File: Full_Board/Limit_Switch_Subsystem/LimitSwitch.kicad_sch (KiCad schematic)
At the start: 7 parts, among them J7 OQ0212500000G

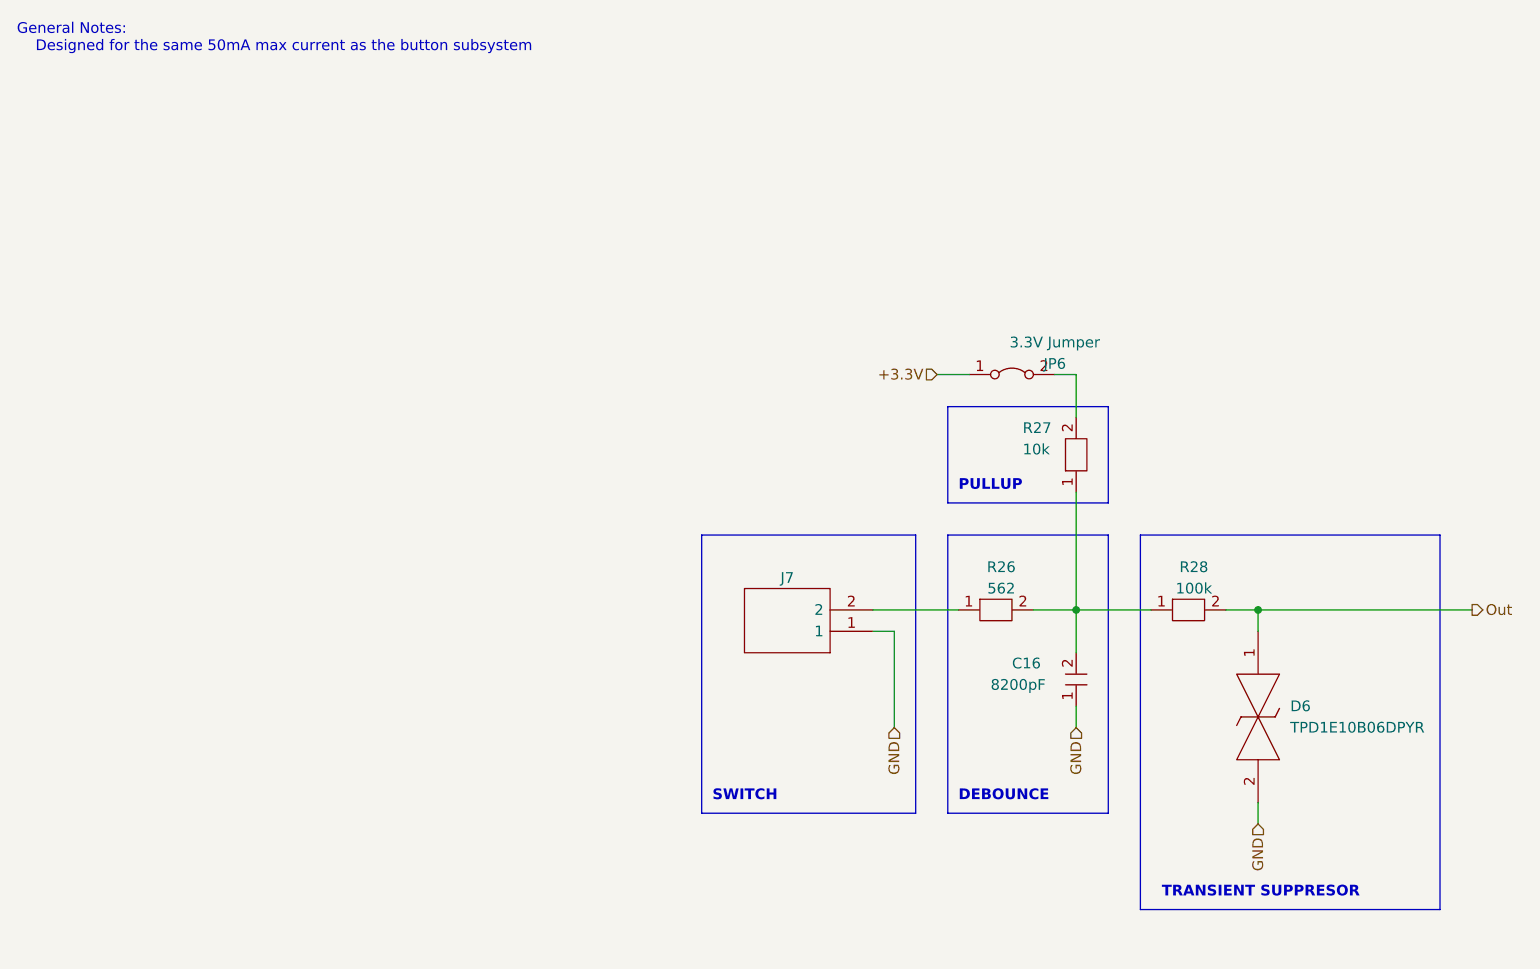
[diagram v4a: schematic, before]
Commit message: Swapped TVS Diodes
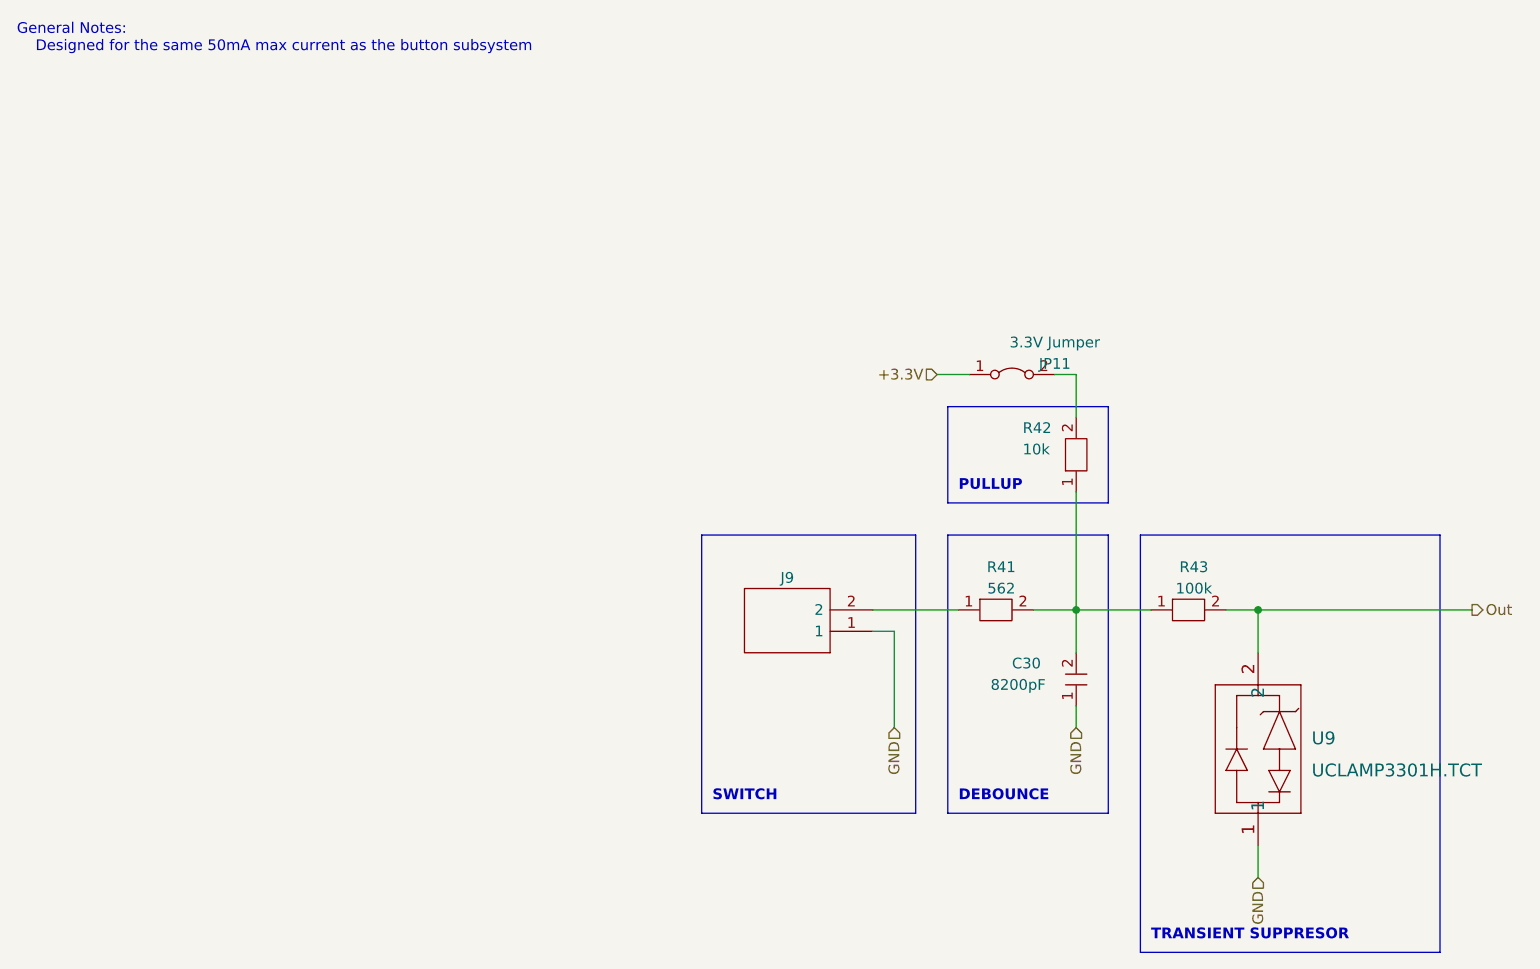
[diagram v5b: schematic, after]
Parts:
- removed D6: TPD1E10B06DPYR, TPD1E10B06DPYR:TPD1E10B06DPYR, symbol TPD1E10B06DPYR:TPD1E10B06DPYR
- added U9: UCLAMP3301H.TCT, SOD_01H.TCT_SEM, symbol UCLAMP3301H-TCT:UCLAMP3301H.TCT
- renumbered C16 to C30, J7 to J9, JP6 to JP11, R26 to R41, R27 to R42, R28 to R43
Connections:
- net GND: now also U9.1
- net Out: now also U9.2
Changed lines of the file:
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@@
     (stroke (width 0) (type default) (color 0 0 0 0))
   )
-  (polyline (pts (xy 151.13 125.73) (xy 186.69 125.73))
+  (polyline (pts (xy 151.13 130.81) (xy 186.69 130.81))
     (stroke (width 0) (type default) (color 0 0 0 0))
   )
@@
     (stroke (width 0) (type default) (color 0 0 0 0))
   )
-  (polyline (pts (xy 151.13 81.28) (xy 151.13 125.73))
+  (wire (pts (xy 165.1 118.11) (xy 165.1 121.92))
+    (stroke (width 0) (type default) (color 0 0 0 0))
+  )
+  (polyline (pts (xy 151.13 81.28) (xy 151.13 130.81))
     (stroke (width 0) (type default) (color 0 0 0 0))
   )
@@
     (stroke (width 0) (type default) (color 0 0 0 0))
   )
-  (wire (pts (xy 165.1 90.17) (xy 165.1 92.71))
-    (stroke (width 0) (type default) (color 0 0 0 0))
-  )
-  (wire (pts (xy 165.1 113.03) (xy 165.1 115.57))
+  (wire (pts (xy 165.1 90.17) (xy 165.1 95.25))
     (stroke (width 0) (type default) (color 0 0 0 0))
   )
@@
     (stroke (width 0) (type default) (color 0 0 0 0))
   )
-  (polyline (pts (xy 186.69 125.73) (xy 186.69 81.28))
+  (polyline (pts (xy 186.69 130.81) (xy 186.69 81.28))
     (stroke (width 0) (type default) (color 0 0 0 0))
   )
@@
     (effects (font (size 1.27 1.27) bold) (justify left bottom))
   )
-  (text "TRANSIENT SUPPRESOR" (at 153.67 124.46 0)
+  (text "TRANSIENT SUPPRESOR" (at 152.4 129.54 0)
     (effects (font (size 1.27 1.27) bold) (justify left bottom))
   )
@@
     (effects (font (size 1.27 1.27)) (justify left))
   )
-  (hierarchical_label "GND" (shape input) (at 165.1 115.57 270)
+  (hierarchical_label "GND" (shape input) (at 165.1 121.92 270)
     (effects (font (size 1.27 1.27)) (justify right))
   )
   (symbol (lib_id "OQ0212500000G:OQ0212500000G") (at 119.38 92.71 180)
     (in_bom yes) (on_board yes)
-    (property "Reference" "J7" (id 0) (at 109.22 86.36 0))
+    (property "Reference" "J9" (id 0) (at 109.22 86.36 0))
     (property "Value" "OQ0212500000G" (id 1) (at 109.22 85.09 0)
       (effects (font (size 1.27 1.27)) hide)
@@
   (symbol (lib_id "CR0402-FX-5620GLF:CR0402-FX-5620GLF") (at 129.54 90.17 0)
     (in_bom yes) (on_board yes)
-    (property "Reference" "R26" (id 0) (at 134.62 85.09 0))
+    (property "Reference" "R41" (id 0) (at 134.62 85.09 0))
     (property "Value" "562" (id 1) (at 134.62 87.63 0))
     (property "Footprint" "CR0402-FX-5620GLF:RESC1005X40N" (id 2) (at 143.51 88.9 0)
@@
   (symbol (lib_id "RMCF1206FT10K0:10k") (at 143.51 76.2 90)
     (in_bom yes) (on_board yes)
-    (property "Reference" "R27" (id 0) (at 137.16 68.58 90)
+    (property "Reference" "R42" (id 0) (at 137.16 68.58 90)
       (effects (font (size 1.27 1.27)) (justify right))
     )
@@
   (symbol (lib_id "RCV2512100KFKEGAT:RCV2512100KFKEGAT") (at 152.4 90.17 0)
     (in_bom yes) (on_board yes)
-    (property "Reference" "R28" (id 0) (at 157.48 85.09 0))
+    (property "Reference" "R43" (id 0) (at 157.48 85.09 0))
     (property "Value" "100k" (id 1) (at 157.48 87.63 0))
     (property "Footprint" "RCV2512100KFKEGAT:RESC6332X70N" (id 2) (at 166.37 88.9 0)
@@
   (symbol (lib_id "C1210C822K2RACAUTO:C1210C822K2RACAUTO") (at 143.51 101.6 90)
     (in_bom yes) (on_board yes)
-    (property "Reference" "C16" (id 0) (at 135.89 96.52 90)
+    (property "Reference" "C30" (id 0) (at 135.89 96.52 90)
       (effects (font (size 1.27 1.27)) (justify right))
     )
@@
   (symbol (lib_id "Jumper:Jumper_2_Bridged") (at 135.89 62.23 0)
     (in_bom yes) (on_board yes)
-    (property "Reference" "JP6" (id 0) (at 140.97 60.96 0))
+    (property "Reference" "JP11" (id 0) (at 140.97 60.96 0))
     (property "Value" "3.3V Jumper" (id 1) (at 140.97 58.42 0))
     (property "Footprint" "TestPoint:TestPoint_2Pads_Pitch2.54mm_Drill0.8mm" (id 2) (at 135.89 62.23 0)
@@
     (pin "2")
   )
-  (symbol (lib_id "TPD1E10B06DPYR:TPD1E10B06DPYR") (at 165.1 92.71 270)
-    (in_bom yes) (on_board yes)
-    (property "Reference" "D6" (id 0) (at 168.91 101.6 90)
-      (effects (font (size 1.27 1.27)) (justify left))
-    )
-    (property "Value" "TPD1E10B06DPYR" (id 1) (at 168.91 104.1399 90)
-      (effects (font (size 1.27 1.27)) (justify left))
-    )
-    (property "Footprint" "TPD1E10B06DPYR:TPD1E10B06DPYR" (id 2) (at 168.91 105.41 0)
-      (effects (font (size 1.27 1.27)) (justify left bottom) hide)
-    )
-    (property "Datasheet" "https://www.ti.com/lit/ds/symlink/tpd1e10b06.pdf?HQS=dis-mous-null-mousermode-dsf-pf-null-wwe&ts=1664782336823&ref_url=https%253A%252F%252Feu.mouser.com%252F" (id 3) (at 166.37 105.41 0)
-      (effects (font (size 1.27 1.27)) (justify left bottom) hide)
-    )
-    (property "Manufacturer's Part Number" "TPD1E10B06DPYR" (id 4) (at 151.13 105.41 0)
-      (effects (font (size 1.27 1.27)) (justify left bottom) hide)
-    )
-    (property "Digikey Part Number" "296-30406-1-ND" (id 5) (at 163.83 105.41 0)
-      (effects (font (size 1.27 1.27)) (justify left bottom) hide)
-    )
-    (property "Mouser Part Number" "595-TPD1E10B06DPYR" (id 6) (at 158.75 105.41 0)
-      (effects (font (size 1.27 1.27)) (justify left bottom) hide)
-    )
-    (property "Digikey link" "https://www.digikey.com/en/products/detail/texas-instruments/TPD1E10B06DPYR/3197744" (id 7) (at 156.21 105.41 0)
-      (effects (font (size 1.27 1.27)) (justify left bottom) hide)
-    )
-    (property "Mouser link" "https://www.mouser.com/ProductDetail/Texas-Instruments/TPD1E10B06DPYR?qs=UFc95S4Z4CaJYpQ4xqTc0g%3D%3D" (id 8) (at 153.67 105.41 0)
-      (effects (font (size 1.27 1.27)) (justify left bottom) hide)
-    )
-    (pin "1")
+  (symbol (lib_id "UCLAMP3301H-TCT:UCLAMP3301H.TCT") (at 165.1 127 90)
+    (in_bom yes) (on_board yes) (fields_autoplaced)
+    (property "Reference" "U9" (id 0) (at 171.45 105.41 90)
+      (effects (font (size 1.524 1.524)) (justify right))
+    )
+    (property "Value" "UCLAMP3301H.TCT" (id 1) (at 171.45 109.22 90)
+      (effects (font (size 1.524 1.524)) (justify right))
+    )
+    (property "Footprint" "SOD_01H.TCT_SEM" (id 2) (at 149.86 104.14 0)
+      (effects (font (size 1.524 1.524)) hide)
+    )
+    (property "Datasheet" "https://semtech.my.salesforce.com/sfc/p/#E0000000JelG/a/44000000MDWf/s0KJxyOHQyYOcvBXVBK9X3X8Cxj1gNltZ2vd2k1S0Wo" (id 3) (at 173.99 125.73 0)
+      (effects (font (size 1.524 1.524)) hide)
+    )
+    (property "Manufacturers Part Number" "UCLAMP3301H.TCT" (id 4) (at 151.13 123.19 0)
+      (effects (font (size 1.27 1.27)) hide)
+    )
+    (property "Digikey Part Number" "UCLAMP3301HDKR-ND" (id 5) (at 153.67 124.46 0)
+      (effects (font (size 1.27 1.27)) hide)
+    )
+    (property "Mouser Part Number" "" (id 6) (at 165.1 127 0)
+      (effects (font (size 1.27 1.27)) hide)
+    )
+    (property "Digikey Link" "https://www.digikey.com/en/products/detail/semtech-corporation/UCLAMP3301H-TCT/1000952" (id 7) (at 173.99 125.73 0)
+      (effects (font (size 1.27 1.27)) hide)
+    )
+    (property "Mouser Link" "" (id 8) (at 165.1 127 0)
+      (effects (font (size 1.27 1.27)) hide)
+    )
+    (pin "1")

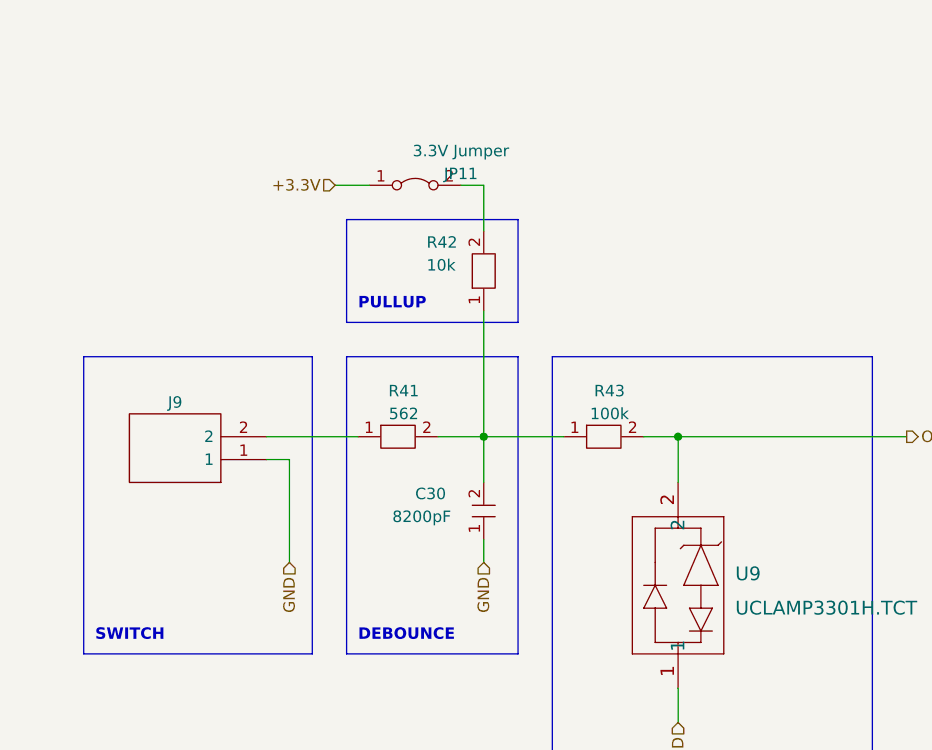
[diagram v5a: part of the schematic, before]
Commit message: Relayed out the power supply and stepper drivers
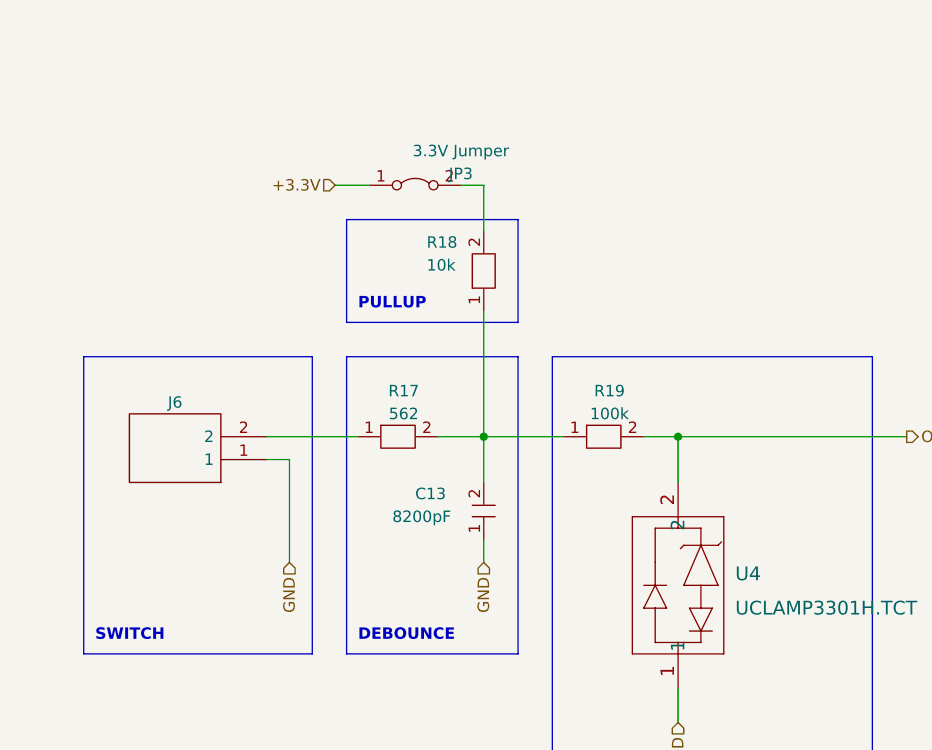
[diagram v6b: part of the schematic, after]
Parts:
- U4: renamed from U9; footprint SOD_01H.TCT_SEM -> UCLAMP3310H-TCT:UCLAMP3301H.TCT
- renumbered C30 to C13, J9 to J6, JP11 to JP3, R41 to R17, R42 to R18, R43 to R19
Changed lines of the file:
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@@
   (symbol (lib_id "OQ0212500000G:OQ0212500000G") (at 119.38 92.71 180)
     (in_bom yes) (on_board yes)
-    (property "Reference" "J9" (id 0) (at 109.22 86.36 0))
+    (property "Reference" "J6" (id 0) (at 109.22 86.36 0))
     (property "Value" "OQ0212500000G" (id 1) (at 109.22 85.09 0)
       (effects (font (size 1.27 1.27)) hide)
@@
   (symbol (lib_id "CR0402-FX-5620GLF:CR0402-FX-5620GLF") (at 129.54 90.17 0)
     (in_bom yes) (on_board yes)
-    (property "Reference" "R41" (id 0) (at 134.62 85.09 0))
+    (property "Reference" "R17" (id 0) (at 134.62 85.09 0))
     (property "Value" "562" (id 1) (at 134.62 87.63 0))
     (property "Footprint" "CR0402-FX-5620GLF:RESC1005X40N" (id 2) (at 143.51 88.9 0)
@@
   (symbol (lib_id "RMCF1206FT10K0:10k") (at 143.51 76.2 90)
     (in_bom yes) (on_board yes)
-    (property "Reference" "R42" (id 0) (at 137.16 68.58 90)
+    (property "Reference" "R18" (id 0) (at 137.16 68.58 90)
       (effects (font (size 1.27 1.27)) (justify right))
     )
@@
   (symbol (lib_id "RCV2512100KFKEGAT:RCV2512100KFKEGAT") (at 152.4 90.17 0)
     (in_bom yes) (on_board yes)
-    (property "Reference" "R43" (id 0) (at 157.48 85.09 0))
+    (property "Reference" "R19" (id 0) (at 157.48 85.09 0))
     (property "Value" "100k" (id 1) (at 157.48 87.63 0))
     (property "Footprint" "RCV2512100KFKEGAT:RESC6332X70N" (id 2) (at 166.37 88.9 0)
@@
   (symbol (lib_id "C1210C822K2RACAUTO:C1210C822K2RACAUTO") (at 143.51 101.6 90)
     (in_bom yes) (on_board yes)
-    (property "Reference" "C30" (id 0) (at 135.89 96.52 90)
+    (property "Reference" "C13" (id 0) (at 135.89 96.52 90)
       (effects (font (size 1.27 1.27)) (justify right))
     )
@@
   (symbol (lib_id "Jumper:Jumper_2_Bridged") (at 135.89 62.23 0)
     (in_bom yes) (on_board yes)
-    (property "Reference" "JP11" (id 0) (at 140.97 60.96 0))
+    (property "Reference" "JP3" (id 0) (at 140.97 60.96 0))
     (property "Value" "3.3V Jumper" (id 1) (at 140.97 58.42 0))
     (property "Footprint" "TestPoint:TestPoint_2Pads_Pitch2.54mm_Drill0.8mm" (id 2) (at 135.89 62.23 0)
@@
   (symbol (lib_id "UCLAMP3301H-TCT:UCLAMP3301H.TCT") (at 165.1 127 90)
     (in_bom yes) (on_board yes) (fields_autoplaced)
-    (property "Reference" "U9" (id 0) (at 171.45 105.41 90)
+    (property "Reference" "U4" (id 0) (at 171.45 105.41 90)
       (effects (font (size 1.524 1.524)) (justify right))
     )
@@
       (effects (font (size 1.524 1.524)) (justify right))
     )
-    (property "Footprint" "SOD_01H.TCT_SEM" (id 2) (at 149.86 104.14 0)
+    (property "Footprint" "UCLAMP3310H-TCT:UCLAMP3301H.TCT" (id 2) (at 149.86 104.14 0)
       (effects (font (size 1.524 1.524)) hide)
     )

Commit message: More layout work
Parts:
- renumbered C13 to C16, J6 to J7, JP3 to JP6, R17 to R26, R18 to R27, R19 to R28, U4 to U7
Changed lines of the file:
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@@
   (symbol (lib_id "OQ0212500000G:OQ0212500000G") (at 119.38 92.71 180)
     (in_bom yes) (on_board yes)
-    (property "Reference" "J6" (id 0) (at 109.22 86.36 0))
+    (property "Reference" "J7" (id 0) (at 109.22 86.36 0))
     (property "Value" "OQ0212500000G" (id 1) (at 109.22 85.09 0)
       (effects (font (size 1.27 1.27)) hide)
@@
   (symbol (lib_id "CR0402-FX-5620GLF:CR0402-FX-5620GLF") (at 129.54 90.17 0)
     (in_bom yes) (on_board yes)
-    (property "Reference" "R17" (id 0) (at 134.62 85.09 0))
+    (property "Reference" "R26" (id 0) (at 134.62 85.09 0))
     (property "Value" "562" (id 1) (at 134.62 87.63 0))
     (property "Footprint" "CR0402-FX-5620GLF:RESC1005X40N" (id 2) (at 143.51 88.9 0)
@@
   (symbol (lib_id "RMCF1206FT10K0:10k") (at 143.51 76.2 90)
     (in_bom yes) (on_board yes)
-    (property "Reference" "R18" (id 0) (at 137.16 68.58 90)
+    (property "Reference" "R27" (id 0) (at 137.16 68.58 90)
       (effects (font (size 1.27 1.27)) (justify right))
     )
@@
   (symbol (lib_id "RCV2512100KFKEGAT:RCV2512100KFKEGAT") (at 152.4 90.17 0)
     (in_bom yes) (on_board yes)
-    (property "Reference" "R19" (id 0) (at 157.48 85.09 0))
+    (property "Reference" "R28" (id 0) (at 157.48 85.09 0))
     (property "Value" "100k" (id 1) (at 157.48 87.63 0))
     (property "Footprint" "RCV2512100KFKEGAT:RESC6332X70N" (id 2) (at 166.37 88.9 0)
@@
   (symbol (lib_id "C1210C822K2RACAUTO:C1210C822K2RACAUTO") (at 143.51 101.6 90)
     (in_bom yes) (on_board yes)
-    (property "Reference" "C13" (id 0) (at 135.89 96.52 90)
+    (property "Reference" "C16" (id 0) (at 135.89 96.52 90)
       (effects (font (size 1.27 1.27)) (justify right))
     )
@@
   (symbol (lib_id "Jumper:Jumper_2_Bridged") (at 135.89 62.23 0)
     (in_bom yes) (on_board yes)
-    (property "Reference" "JP3" (id 0) (at 140.97 60.96 0))
+    (property "Reference" "JP6" (id 0) (at 140.97 60.96 0))
     (property "Value" "3.3V Jumper" (id 1) (at 140.97 58.42 0))
     (property "Footprint" "TestPoint:TestPoint_2Pads_Pitch2.54mm_Drill0.8mm" (id 2) (at 135.89 62.23 0)
@@
   (symbol (lib_id "UCLAMP3301H-TCT:UCLAMP3301H.TCT") (at 165.1 127 90)
     (in_bom yes) (on_board yes) (fields_autoplaced)
-    (property "Reference" "U4" (id 0) (at 171.45 105.41 90)
+    (property "Reference" "U7" (id 0) (at 171.45 105.41 90)
       (effects (font (size 1.524 1.524)) (justify right))
     )
